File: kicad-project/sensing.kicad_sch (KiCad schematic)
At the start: 11 parts

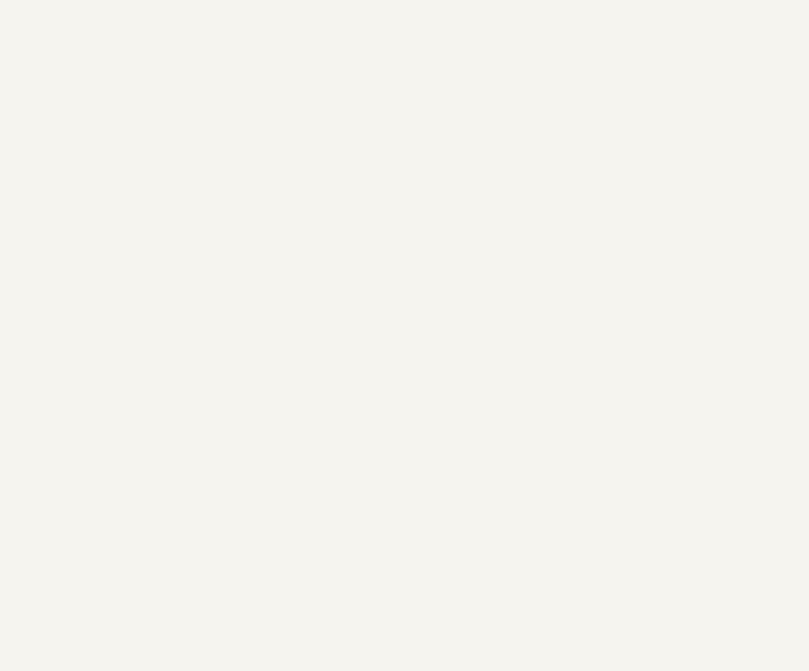
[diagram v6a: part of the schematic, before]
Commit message: hw: move inputs from control to sensing and outputs from control to actuation
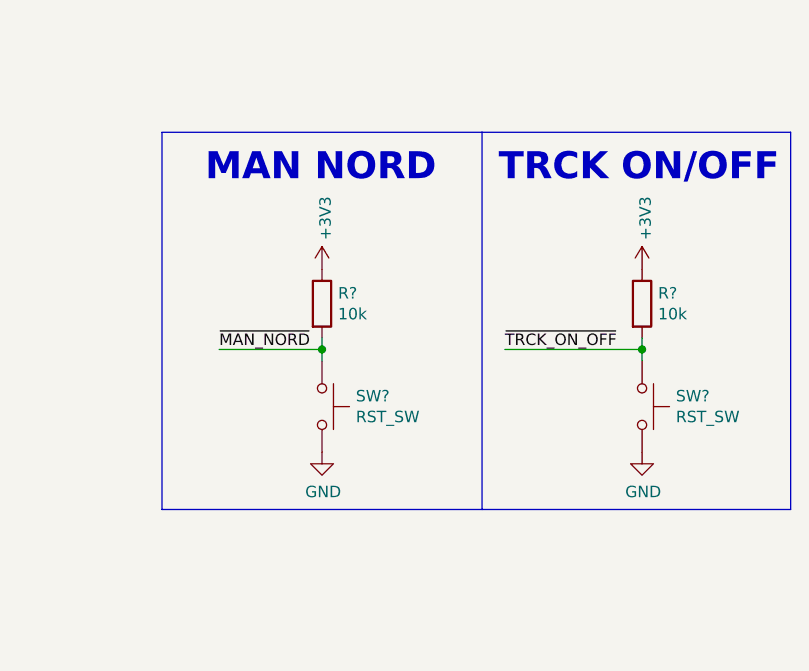
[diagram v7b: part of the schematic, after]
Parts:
- added R? (x2): 10k, symbol Device:R
- added SW? (x2): RST_SW, symbol Switch:SW_Push
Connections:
- net +3V3: now also R?.1, R?.1
- net GND: now also SW?.2, SW?.2
- new net ~{MAN_NORD}: R?.2, SW?.1
- new net ~{TRCK_ON_OFF}: R?.2, SW?.1
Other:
- note added: "MAN NORD"
- note added: "TRCK ON/OFF"
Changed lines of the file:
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@@
   (junction (at 46.99 49.53) (diameter 0) (color 0 0 0 0)
   )
+  (junction (at 205.74 50.8) (diameter 0) (color 0 0 0 0)
+  )
   (junction (at 60.96 97.79) (diameter 0) (color 0 0 0 0)
   )
@@
   (junction (at 64.77 52.07) (diameter 0) (color 0 0 0 0)
   )
+  (junction (at 241.3 50.8) (diameter 0) (color 0 0 0 0)
+  )
   (junction (at 137.16 54.61) (diameter 0) (color 0 0 0 0)
   )
@@
     (stroke (width 0) (type default) (color 0 0 0 0))
   )
+  (polyline (pts (xy 257.81 26.67) (xy 257.81 68.58))
+    (stroke (width 0) (type default) (color 0 0 0 0))
+  )
   (wire (pts (xy 49.53 68.58) (xy 46.99 68.58))
     (stroke (width 0) (type default) (color 0 0 0 0))
@@
     (stroke (width 0) (type default) (color 0 0 0 0))
   )
+  (polyline (pts (xy 187.96 68.58) (xy 187.96 26.67))
+    (stroke (width 0) (type default) (color 0 0 0 0))
+  )
   (polyline (pts (xy 86.36 78.74) (xy 86.36 13.97))
     (stroke (width 0) (type default) (color 0 0 0 0))
   )
+  (wire (pts (xy 241.3 49.53) (xy 241.3 50.8))
+    (stroke (width 0) (type default) (color 0 0 0 0))
+  )
+  (polyline (pts (xy 223.52 26.67) (xy 257.81 26.67))
+    (stroke (width 0) (type default) (color 0 0 0 0))
+  )
+  (polyline (pts (xy 187.96 26.67) (xy 223.52 26.67))
+    (stroke (width 0) (type default) (color 0 0 0 0))
+  )
   (polyline (pts (xy 13.97 78.74) (xy 13.97 13.97))
     (stroke (width 0) (type default) (color 0 0 0 0))
@@
     (stroke (width 0) (type default) (color 0 0 0 0))
   )
+  (polyline (pts (xy 223.52 68.58) (xy 257.81 68.58))
+    (stroke (width 0) (type default) (color 0 0 0 0))
+  )
   (polyline (pts (xy 86.36 13.97) (xy 157.48 13.97))
     (stroke (width 0) (type default) (color 0 0 0 0))
@@
     (stroke (width 0) (type default) (color 0 0 0 0))
   )
+  (polyline (pts (xy 187.96 68.58) (xy 223.52 68.58))
+    (stroke (width 0) (type default) (color 0 0 0 0))
+  )
   (wire (pts (xy 64.77 68.58) (xy 64.77 52.07))
     (stroke (width 0) (type default) (color 0 0 0 0))
@@
     (stroke (width 0) (type default) (color 0 0 0 0))
   )
+  (polyline (pts (xy 223.52 68.58) (xy 223.52 26.67))
+    (stroke (width 0) (type default) (color 0 0 0 0))
+  )
   (polyline (pts (xy 86.36 78.74) (xy 13.97 78.74))
     (stroke (width 0) (type default) (color 0 0 0 0))
   )
+  (wire (pts (xy 241.3 50.8) (xy 241.3 52.07))
+    (stroke (width 0) (type default) (color 0 0 0 0))
+  )
+  (wire (pts (xy 205.74 50.8) (xy 205.74 52.07))
+    (stroke (width 0) (type default) (color 0 0 0 0))
+  )
   (wire (pts (xy 49.53 35.56) (xy 46.99 35.56))
     (stroke (width 0) (type default) (color 0 0 0 0))
@@
     (stroke (width 0) (type default) (color 0 0 0 0))
   )
+  (wire (pts (xy 205.74 49.53) (xy 205.74 50.8))
+    (stroke (width 0) (type default) (color 0 0 0 0))
+  )
   (wire (pts (xy 64.77 52.07) (xy 68.58 52.07))
     (stroke (width 0) (type default) (color 0 0 0 0))
@@
     (stroke (width 0) (type default) (color 0 0 0 0))
   )
+  (wire (pts (xy 226.06 50.8) (xy 241.3 50.8))
+    (stroke (width 0) (type default) (color 0 0 0 0))
+  )
   (wire (pts (xy 60.96 95.25) (xy 60.96 97.79))
     (stroke (width 0) (type default) (color 0 0 0 0))
@@
     (stroke (width 0) (type default) (color 0 0 0 0))
   )
+  (wire (pts (xy 194.31 50.8) (xy 205.74 50.8))
+    (stroke (width 0) (type default) (color 0 0 0 0))
+  )
   (polyline (pts (xy 157.48 78.74) (xy 157.48 13.97))
     (stroke (width 0) (type default) (color 0 0 0 0))
+  )
+  (text "TRCK ON/OFF" (at 256.54 32.385 180)
+    (effects (font (size 3 3) (thickness 0.6) bold) (justify right bottom))
   )
   (text "Values need to be determined when the solar panel is defined"
@@
     (effects (font (size 1.27 1.27)) (justify left bottom))
   )
+  (text "MAN NORD" (at 218.44 32.385 180)
+    (effects (font (size 3 3) (thickness 0.6) bold) (justify right bottom))
+  )
   (text "Current sensing" (at 31.75 19.685 0)
     (effects (font (size 3 3) (thickness 0.6) bold) (justify left bottom))
@@
     (effects (font (size 1.27 1.27)) (justify right bottom))
   )
+  (label "~{MAN_NORD}" (at 194.31 50.8 0)
+    (effects (font (size 1.27 1.27)) (justify left bottom))
+  )
   (label "Panel IN -" (at 55.88 100.33 180)
     (effects (font (size 1.27 1.27)) (justify right bottom))
@@
   (label "Panel IN +" (at 105.41 31.75 270)
     (effects (font (size 1.27 1.27)) (justify right bottom))
+  )
+  (label "~{TRCK_ON_OFF}" (at 226.06 50.8 0)
+    (effects (font (size 1.27 1.27)) (justify left bottom))
   )
   (label "Panel OUT -" (at 55.88 95.25 180)
@@
     )
     (property "Datasheet" "" (id 3) (at 105.41 60.96 0)
+      (effects (font (size 1.27 1.27)) hide)
+    )
+    (pin "1")
+  )
+  (symbol (lib_id "power:GND") (at 241.3 62.23 0) (unit 1)
+    (in_bom yes) (on_board yes)
+    (property "Reference" "#PWR?" (id 0) (at 241.3 68.58 0)
+      (effects (font (size 1.27 1.27)) hide)
+    )
+    (property "Value" "GND" (id 1) (at 241.427 66.6242 0))
+    (property "Footprint" "" (id 2) (at 241.3 62.23 0)
+      (effects (font (size 1.27 1.27)) hide)
+    )
+    (property "Datasheet" "" (id 3) (at 241.3 62.23 0)
       (effects (font (size 1.27 1.27)) hide)
     )
@@
     (pin "1")
   )
+  (symbol (lib_id "power:+3V3") (at 241.3 41.91 0) (unit 1)
+    (in_bom yes) (on_board yes)
+    (property "Reference" "#PWR?" (id 0) (at 241.3 45.72 0)
+      (effects (font (size 1.27 1.27)) hide)
+    )
+    (property "Value" "+3V3" (id 1) (at 241.681 38.6588 90)
+      (effects (font (size 1.27 1.27)) (justify left))
+    )
+    (property "Footprint" "" (id 2) (at 241.3 41.91 0)
+      (effects (font (size 1.27 1.27)) hide)
+    )
+    (property "Datasheet" "" (id 3) (at 241.3 41.91 0)
+      (effects (font (size 1.27 1.27)) hide)
+    )
+    (pin "1")
+  )
   (symbol (lib_id "power:+3V3") (at 53.34 44.45 0) (unit 1)
     (in_bom yes) (on_board yes)
@@
     (pin "2")
   )
+  (symbol (lib_id "power:+3V3") (at 205.74 41.91 0) (unit 1)
+    (in_bom yes) (on_board yes)
+    (property "Reference" "#PWR?" (id 0) (at 205.74 45.72 0)
+      (effects (font (size 1.27 1.27)) hide)
+    )
+    (property "Value" "+3V3" (id 1) (at 206.121 38.6588 90)
+      (effects (font (size 1.27 1.27)) (justify left))
+    )
+    (property "Footprint" "" (id 2) (at 205.74 41.91 0)
+      (effects (font (size 1.27 1.27)) hide)
+    )
+    (property "Datasheet" "" (id 3) (at 205.74 41.91 0)
+      (effects (font (size 1.27 1.27)) hide)
+    )
+    (pin "1")
+  )
   (symbol (lib_id "Device:R") (at 105.41 46.99 0) (unit 1)
     (in_bom yes) (on_board yes) (fields_autoplaced)
@@
     (pin "2")
   )
+  (symbol (lib_id "Device:R") (at 205.74 45.72 0) (unit 1)
+    (in_bom yes) (on_board yes)
+    (property "Reference" "R?" (id 0) (at 207.518 44.5516 0)
+      (effects (font (size 1.27 1.27)) (justify left))
+    )
+    (property "Value" "10k" (id 1) (at 207.518 46.863 0)
+      (effects (font (size 1.27 1.27)) (justify left))
+    )
+    (property "Footprint" "" (id 2) (at 203.962 45.72 90)
+      (effects (font (size 1.27 1.27)) hide)
+    )
+    (property "Datasheet" "~" (id 3) (at 205.74 45.72 0)
+      (effects (font (size 1.27 1.27)) hide)
+    )
+    (pin "1")
+    (pin "2")
+  )
+  (symbol (lib_id "Switch:SW_Push") (at 241.3 57.15 270) (unit 1)
+    (in_bom yes) (on_board yes)
+    (property "Reference" "SW?" (id 0) (at 245.0592 55.9816 90)
+      (effects (font (size 1.27 1.27)) (justify left))
+    )
+    (property "Value" "RST_SW" (id 1) (at 245.0592 58.293 90)
+      (effects (font (size 1.27 1.27)) (justify left))
+    )
+    (property "Footprint" "" (id 2) (at 246.38 57.15 0)
+      (effects (font (size 1.27 1.27)) hide)
+    )
+    (property "Datasheet" "~" (id 3) (at 246.38 57.15 0)
+      (effects (font (size 1.27 1.27)) hide)
+    )
+    (pin "1")
+    (pin "2")
+  )
+  (symbol (lib_id "Switch:SW_Push") (at 205.74 57.15 270) (unit 1)
+    (in_bom yes) (on_board yes)
+    (property "Reference" "SW?" (id 0) (at 209.4992 55.9816 90)
+      (effects (font (size 1.27 1.27)) (justify left))
+    )
+    (property "Value" "RST_SW" (id 1) (at 209.4992 58.293 90)
+      (effects (font (size 1.27 1.27)) (justify left))
+    )
+    (property "Footprint" "" (id 2) (at 210.82 57.15 0)
+      (effects (font (size 1.27 1.27)) hide)
+    )
+    (property "Datasheet" "~" (id 3) (at 210.82 57.15 0)
+      (effects (font (size 1.27 1.27)) hide)
+    )
+    (pin "1")
+    (pin "2")
+  )
   (symbol (lib_id "Device:R") (at 53.34 35.56 90) (unit 1)
     (in_bom yes) (on_board yes)
@@
     )
     (property "Datasheet" "" (id 3) (at 60.96 97.79 0)
+      (effects (font (size 1.27 1.27)) hide)
+    )
+    (pin "1")
+  )
+  (symbol (lib_id "power:GND") (at 205.74 62.23 0) (unit 1)
+    (in_bom yes) (on_board yes)
+    (property "Reference" "#PWR?" (id 0) (at 205.74 68.58 0)
+      (effects (font (size 1.27 1.27)) hide)
+    )
+    (property "Value" "GND" (id 1) (at 205.867 66.6242 0))
+    (property "Footprint" "" (id 2) (at 205.74 62.23 0)
+      (effects (font (size 1.27 1.27)) hide)
+    )
+    (property "Datasheet" "" (id 3) (at 205.74 62.23 0)
       (effects (font (size 1.27 1.27)) hide)
     )
@@
     (pin "4")
   )
+  (symbol (lib_id "Device:R") (at 241.3 45.72 0) (unit 1)
+    (in_bom yes) (on_board yes)
+    (property "Reference" "R?" (id 0) (at 243.078 44.5516 0)
+      (effects (font (size 1.27 1.27)) (justify left))
+    )
+    (property "Value" "10k" (id 1) (at 243.078 46.863 0)
+      (effects (font (size 1.27 1.27)) (justify left))
+    )
+    (property "Footprint" "" (id 2) (at 239.522 45.72 90)
+      (effects (font (size 1.27 1.27)) hide)
+    )
+    (property "Datasheet" "~" (id 3) (at 241.3 45.72 0)
+      (effects (font (size 1.27 1.27)) hide)
+    )
+    (pin "1")
+    (pin "2")
+  )
   (symbol (lib_id "power:+3V3") (at 125.73 46.99 0) (unit 1)

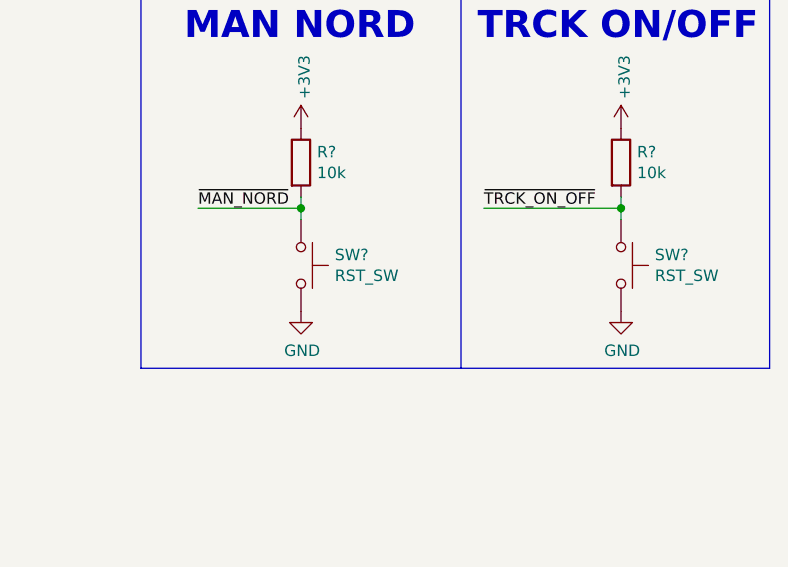
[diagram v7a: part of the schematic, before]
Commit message: fw: discrete dirver for stepper
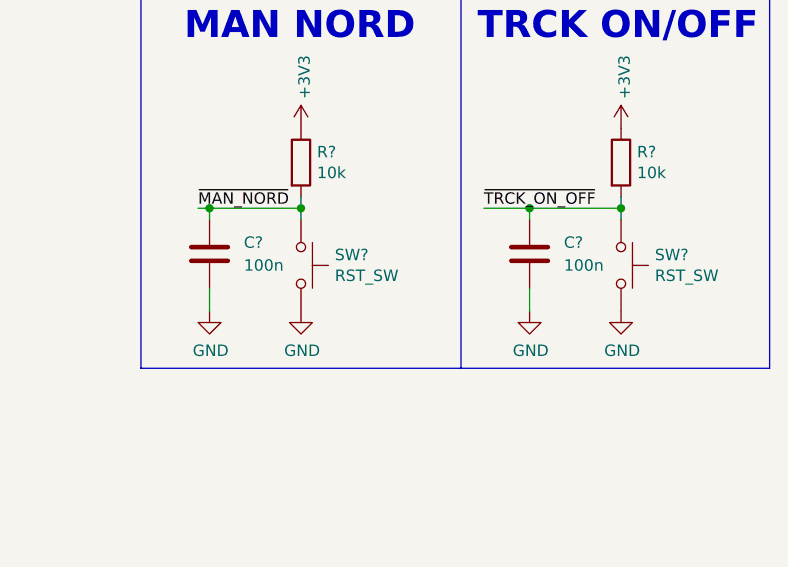
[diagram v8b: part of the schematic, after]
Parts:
- added C? (x2): 100n, symbol Device:C
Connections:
- net GND: now also C?.2, C?.2
- net ~{MAN_NORD}: now also C?.1
- net ~{TRCK_ON_OFF}: now also C?.1
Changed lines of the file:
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@@
     (title "Sensing")
   )
+  (junction (at 231.14 50.8) (diameter 0) (color 0 0 0 0)
+  )
+  (junction (at 195.58 50.8) (diameter 0) (color 0 0 0 0)
+  )
   (junction (at 105.41 52.07) (diameter 0) (color 0 0 0 0)
   )
@@
     (stroke (width 0) (type default) (color 0 0 0 0))
   )
+  (wire (pts (xy 195.58 50.8) (xy 195.58 52.07))
+    (stroke (width 0) (type default) (color 0 0 0 0))
+  )
   (polyline (pts (xy 86.36 109.22) (xy 86.36 78.74))
     (stroke (width 0) (type default) (color 0 0 0 0))
@@
     (stroke (width 0) (type default) (color 0 0 0 0))
   )
+  (wire (pts (xy 195.58 50.8) (xy 205.74 50.8))
+    (stroke (width 0) (type default) (color 0 0 0 0))
+  )
   (wire (pts (xy 105.41 43.18) (xy 105.41 31.75))
     (stroke (width 0) (type default) (color 0 0 0 0))
@@
     (stroke (width 0) (type default) (color 0 0 0 0))
   )
+  (wire (pts (xy 231.14 50.8) (xy 241.3 50.8))
+    (stroke (width 0) (type default) (color 0 0 0 0))
+  )
   (wire (pts (xy 33.02 49.53) (xy 35.56 49.53))
     (stroke (width 0) (type default) (color 0 0 0 0))
@@
     (stroke (width 0) (type default) (color 0 0 0 0))
   )
-  (wire (pts (xy 226.06 50.8) (xy 241.3 50.8))
+  (wire (pts (xy 226.06 50.8) (xy 231.14 50.8))
     (stroke (width 0) (type default) (color 0 0 0 0))
   )
@@
     (stroke (width 0) (type default) (color 0 0 0 0))
   )
+  (wire (pts (xy 231.14 59.69) (xy 231.14 62.23))
+    (stroke (width 0) (type default) (color 0 0 0 0))
+  )
+  (wire (pts (xy 195.58 59.69) (xy 195.58 62.23))
+    (stroke (width 0) (type default) (color 0 0 0 0))
+  )
   (wire (pts (xy 29.21 57.15) (xy 29.21 69.85))
     (stroke (width 0) (type default) (color 0 0 0 0))
@@
     (stroke (width 0) (type default) (color 0 0 0 0))
   )
+  (wire (pts (xy 231.14 50.8) (xy 231.14 52.07))
+    (stroke (width 0) (type default) (color 0 0 0 0))
+  )
   (wire (pts (xy 43.18 49.53) (xy 46.99 49.53))
     (stroke (width 0) (type default) (color 0 0 0 0))
   )
-  (wire (pts (xy 194.31 50.8) (xy 205.74 50.8))
+  (wire (pts (xy 194.31 50.8) (xy 195.58 50.8))
     (stroke (width 0) (type default) (color 0 0 0 0))
   )
@@
     (pin "1")
   )
+  (symbol (lib_id "power:GND") (at 195.58 62.23 0) (unit 1)
+    (in_bom yes) (on_board yes)
+    (property "Reference" "#PWR?" (id 0) (at 195.58 68.58 0)
+      (effects (font (size 1.27 1.27)) hide)
+    )
+    (property "Value" "GND" (id 1) (at 195.707 66.6242 0))
+    (property "Footprint" "" (id 2) (at 195.58 62.23 0)
+      (effects (font (size 1.27 1.27)) hide)
+    )
+    (property "Datasheet" "" (id 3) (at 195.58 62.23 0)
+      (effects (font (size 1.27 1.27)) hide)
+    )
+    (pin "1")
+  )
+  (symbol (lib_id "Device:C") (at 195.58 55.88 0) (unit 1)
+    (in_bom yes) (on_board yes) (fields_autoplaced)
+    (property "Reference" "C?" (id 0) (at 199.39 54.6099 0)
+      (effects (font (size 1.27 1.27)) (justify left))
+    )
+    (property "Value" "100n" (id 1) (at 199.39 57.1499 0)
+      (effects (font (size 1.27 1.27)) (justify left))
+    )
+    (property "Footprint" "" (id 2) (at 196.5452 59.69 0)
+      (effects (font (size 1.27 1.27)) hide)
+    )
+    (property "Datasheet" "~" (id 3) (at 195.58 55.88 0)
+      (effects (font (size 1.27 1.27)) hide)
+    )
+    (pin "1")
+    (pin "2")
+  )
   (symbol (lib_id "Device:R") (at 105.41 57.15 0) (unit 1)
     (in_bom yes) (on_board yes) (fields_autoplaced)
@@
     (pin "1")
     (pin "2")
+  )
+  (symbol (lib_id "power:GND") (at 231.14 62.23 0) (unit 1)
+    (in_bom yes) (on_board yes)
+    (property "Reference" "#PWR?" (id 0) (at 231.14 68.58 0)
+      (effects (font (size 1.27 1.27)) hide)
+    )
+    (property "Value" "GND" (id 1) (at 231.267 66.6242 0))
+    (property "Footprint" "" (id 2) (at 231.14 62.23 0)
+      (effects (font (size 1.27 1.27)) hide)
+    )
+    (property "Datasheet" "" (id 3) (at 231.14 62.23 0)
+      (effects (font (size 1.27 1.27)) hide)
+    )
+    (pin "1")
   )
   (symbol (lib_id "Device:R") (at 39.37 54.61 90) (unit 1)
@@
       (effects (font (size 1.27 1.27)) hide)
     )
+    (pin "1")
+    (pin "2")
+  )
+  (symbol (lib_id "Device:C") (at 231.14 55.88 0) (unit 1)
+    (in_bom yes) (on_board yes) (fields_autoplaced)
+    (property "Reference" "C?" (id 0) (at 234.95 54.6099 0)
+      (effects (font (size 1.27 1.27)) (justify left))
+    )
+    (property "Value" "100n" (id 1) (at 234.95 57.1499 0)
+      (effects (font (size 1.27 1.27)) (justify left))
+    )
+    (property "Footprint" "" (id 2) (at 232.1052 59.69 0)
+      (effects (font (size 1.27 1.27)) hide)
+    )
+    (property "Datasheet" "~" (id 3) (at 231.14 55.88 0)
+      (effects (font (size 1.27 1.27)) hide)
+    )
